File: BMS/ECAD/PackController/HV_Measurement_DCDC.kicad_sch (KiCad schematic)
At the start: 16 parts, among them U2002 TEA1-0505HI

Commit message: finalised schematic of pack controller
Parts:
- removed C2015: 100n 0603 50V, symbol Device:C
- removed U2005: (no value), symbol EKartParts:ADCMP393ARUZ
- C2001: footprint (none) -> Capacitor_SMD:C_0805_2012Metric
- C2009: footprint (none) -> Capacitor_SMD:C_0603_1608Metric
- R2003: footprint (none) -> Resistor_SMD:R_2512_6332Metric_Pad1.40x3.35mm_HandSolder
- U2001: value (none) -> ADUM3190; footprint (none) -> Package_SO:QSOP-16_3.9x4.9mm_P0.635mm

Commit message: many fixes
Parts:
- removed C2001, C2011, C2013: 1uC 0805 50V, Capacitor_SMD:C_0805_2012Metric, symbol Device:C
- removed C2009: 100n 0603 50V, Capacitor_SMD:C_0603_1608Metric, symbol Device:C
- removed R2002: 4.7MR 2512 3kV 1%, Resistor_SMD:R_2512_6332Metric_Pad1.40x3.35mm_HandSolder, symbol Device:R
- removed R2003: 39kR 2512 500V 1%, Resistor_SMD:R_2512_6332Metric_Pad1.40x3.35mm_HandSolder, symbol Device:R
- removed R2007, R2009: 10kR, Resistor_SMD:R_0603_1608Metric_Pad0.98x0.95mm_HandSolder, symbol Device:R
- removed U2001: ADUM3190, Package_SO:QSOP-16_3.9x4.9mm_P0.635mm, symbol EKartParts:ADUM3190
- added C2002, C2006: 100nC 0603 50V, Capacitor_SMD:C_0603_1608Metric, symbol Device:C
- added C2004: 100pC 0603 50V, Capacitor_SMD:C_0603_1608Metric, symbol Device:C
- added C2008: 100nC 0603 16V, Capacitor_SMD:C_0603_1608Metric, symbol Device:C
- added C2010: 1uC 0805 50V, Capacitor_SMD:C_0805_2012Metric, symbol Device:C
- added C2012: 1uC 0805 16V, Capacitor_SMD:C_0805_2012Metric, symbol Device:C
- added C2014: 1nC 0603 16V, Capacitor_SMD:C_0603_1608Metric, symbol Device:C
- added C2015: 100nF 0603 100V, Capacitor_SMD:C_0603_1608Metric_Pad1.08x0.95mm_HandSolder, symbol Device:C
- added C2016: 1uF 0805 50V, Capacitor_SMD:C_0805_2012Metric, symbol Device:C
- added R2004, R2005: 4.7MR 2512 3kV 0,1%, Resistor_SMD:R_2512_6332Metric_Pad1.40x3.35mm_HandSolder, symbol Device:R
- added R2006: 26.1kR 2512 500V 0,1%, Resistor_SMD:R_2512_6332Metric_Pad1.40x3.35mm_HandSolder, symbol Device:R
- added R2008: 1kR, Resistor_SMD:R_0603_1608Metric_Pad0.98x0.95mm_HandSolder, symbol Device:R
- added U2003: AMC0311R, EKartParts:AMC0311R Wide-body SOIC (DWV), symbol EKartParts:AMC0311R
- added U2004: LP5907MFX-3.3, Package_TO_SOT_SMD:SOT-23-5, symbol Regulator_Linear:LP5907MFX-3.3
- R2001: value 4.7MR 2512 3kV 1% -> 500R 0805; footprint Resistor_SMD:R_2512_6332Metric_Pad1.40x3.35mm_HandSolder -> Resistor_SMD:R_0805_2012Metric_Pad1.20x1.40mm_HandSolder
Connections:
- net +5V_VEHI is gone; now on net +5V_DCDC: C2003.2, C2005.1, U2002.7 (+Vout)
- net +3.3V: now also C2006.1, U2003.6 (REFIN)
- net +5V: now also C2008.1, C2012.1, U2003.8 (VDD2)
- net +5V_DCDC: now also R2001.2, U2004.1 (IN), U2004.3 (EN)
- net GND: now also C2007.2, U2002.2 (-Vin), C2006.2, C2008.2, C2012.2, C2014.2, U2003.5 (GND2)
- net TS_N_ACCU: now also R2001.1, C2002.2, C2004.2, C2010.2, C2015.1, C2016.2, R2006.2, U2003.3 (SNSN), U2003.4 (GND1), U2004.2 (GND)
- net TS_P_DCDC: now also R2004.1; no longer R2001.1
- net V_DCDC: now also C2014.1, R2008.1
- new net: R2004.2, R2005.1
- new net: C2004.1, R2005.2, R2006.1, U2003.2 (INP)
- new net: R2008.2, U2003.7 (OUT)
- new net +3.3V_DCDC: C2002.1, C2010.1, C2015.2, C2016.1, U2003.1 (VDD1), U2004.5 (OUT)
- no-connect marks 3 -> 0
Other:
- moved on the sheet: C2003, C2005, C2007, U2002

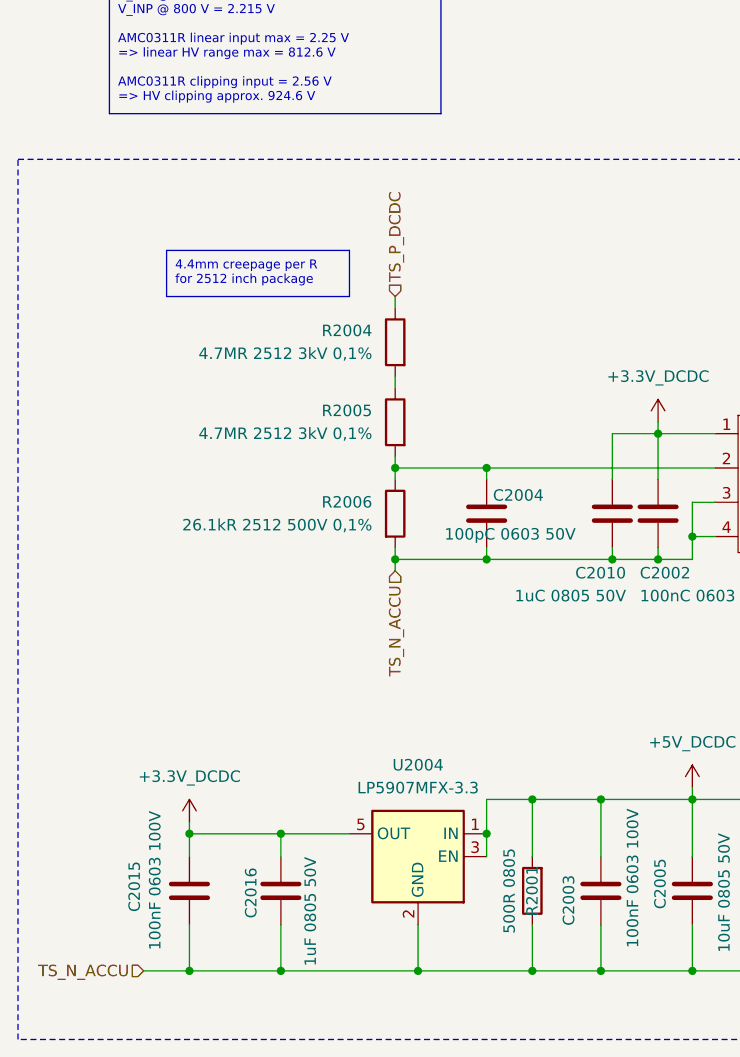
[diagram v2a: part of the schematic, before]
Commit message: add rule areas for hv separation
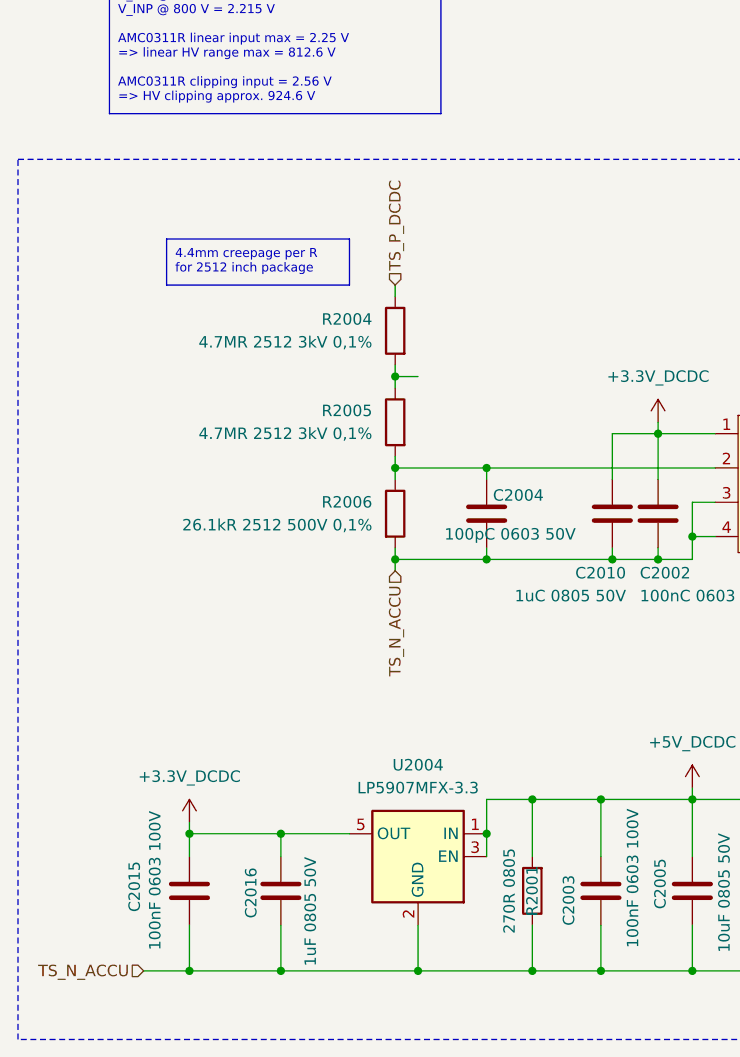
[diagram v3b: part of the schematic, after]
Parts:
- R2001: value 500R 0805 -> 270R 0805
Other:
- moved on the sheet: R2004
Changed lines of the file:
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@@
 	(text_box "4.4mm creepage per R for 2512 inch package"
 		(exclude_from_sim no)
-		(at 50.8 79.9663 0)
+		(at 50.8 78.6963 0)
 		(size 20.32 5.1237)
 		(margins 0.9525 0.9525 0.9525 0.9525)
@@
 	)
 	(junction
+		(at 76.2 93.98)
+		(diameter 0)
+		(color 0 0 0 0)
+	)
+	(junction
 		(at 109.22 140.97)
 		(diameter 0)
@@
 	(wire
 		(pts
-			(xy 76.2 85.09) (xy 76.2 86.36)
+			(xy 76.2 83.82) (xy 76.2 85.09)
 		)
 		(stroke
@@
 	(wire
 		(pts
+			(xy 76.2 93.98) (xy 78.74 93.98)
+		)
+		(stroke
+			(width 0)
+			(type default)
+		)
+	)
+	(wire
+		(pts
 			(xy 138.43 153.67) (xy 137.16 153.67)
 		)
@@
 		(pts
 			(xy 147.32 100.33) (xy 152.4 100.33)
+		)
+		(stroke
+			(width 0)
+			(type default)
+		)
+	)
+	(wire
+		(pts
+			(xy 76.2 92.71) (xy 76.2 93.98)
 		)
 		(stroke
@@
 	(hierarchical_label "TS_P_DCDC"
 		(shape input)
-		(at 76.2 85.09 90)
+		(at 76.2 83.82 90)
 		(effects
 			(font
@@
 			)
 			(justify left)
+		)
+	)
+	(netclass_flag ""
+		(length 2.54)
+		(shape round)
+		(at 86.36 104.14 0)
+		(fields_autoplaced yes)
+		(effects
+			(font
+				(size 1.27 1.27)
+			)
+			(justify left bottom)
+		)
+		(property "Netzklasse" "HV0"
+			(at 87.0585 101.6 0)
+			(show_name no)
+			(do_not_autoplace no)
+			(effects
+				(font
+					(size 1.27 1.27)
+				)
+				(justify left)
+			)
+		)
+		(property "Component Class" ""
+			(at 63.5 25.4 0)
+			(show_name no)
+			(do_not_autoplace no)
+			(effects
+				(font
+					(size 1.27 1.27)
+					(italic yes)
+				)
+			)
+		)
+	)
+	(netclass_flag ""
+		(length 2.54)
+		(shape round)
+		(at 78.74 93.98 0)
+		(fields_autoplaced yes)
+		(effects
+			(font
+				(size 1.27 1.27)
+			)
+			(justify left bottom)
+		)
+		(property "Netzklasse" "HV400"
+			(at 79.4385 91.44 0)
+			(show_name no)
+			(do_not_autoplace no)
+			(effects
+				(font
+					(size 1.27 1.27)
+				)
+				(justify left)
+			)
+		)
+		(property "Component Class" ""
+			(at 55.88 15.24 0)
+			(show_name no)
+			(do_not_autoplace no)
+			(effects
+				(font
+					(size 1.27 1.27)
+					(italic yes)
+				)
+			)
+		)
+	)
+	(netclass_flag ""
+		(length 2.54)
+		(shape round)
+		(at 63.5 144.78 0)
+		(fields_autoplaced yes)
+		(effects
+			(font
+				(size 1.27 1.27)
+			)
+			(justify left bottom)
+		)
+		(property "Netzklasse" "HV0"
+			(at 64.1985 142.24 0)
+			(show_name no)
+			(do_not_autoplace no)
+			(effects
+				(font
+					(size 1.27 1.27)
+				)
+				(justify left)
+			)
+		)
+		(property "Component Class" ""
+			(at 40.64 66.04 0)
+			(show_name no)
+			(do_not_autoplace no)
+			(effects
+				(font
+					(size 1.27 1.27)
+					(italic yes)
+				)
+			)
+		)
+	)
+	(netclass_flag ""
+		(length 2.54)
+		(shape round)
+		(at 99.06 140.97 0)
+		(fields_autoplaced yes)
+		(effects
+			(font
+				(size 1.27 1.27)
+			)
+			(justify left bottom)
+		)
+		(property "Netzklasse" "HV0"
+			(at 99.7585 138.43 0)
+			(show_name no)
+			(do_not_autoplace no)
+			(effects
+				(font
+					(size 1.27 1.27)
+				)
+				(justify left)
+			)
+		)
+		(property "Component Class" ""
+			(at 76.2 62.23 0)
+			(show_name no)
+			(do_not_autoplace no)
+			(effects
+				(font
+					(size 1.27 1.27)
+					(italic yes)
+				)
+			)
 		)
 	)
@@
 	(symbol
 		(lib_id "Device:R")
-		(at 76.2 90.17 0)
+		(at 76.2 88.9 0)
 		(mirror y)
 		(unit 1)
@@
 		(fields_autoplaced yes)
 		(property "Reference" "R2004"
-			(at 73.66 88.8999 0)
+			(at 73.66 87.6299 0)
 			(show_name no)
 			(do_not_autoplace no)
@@
 		)
 		(property "Value" "4.7MR 2512 3kV 0,1%"
-			(at 73.66 91.4399 0)
+			(at 73.66 90.1699 0)
 			(show_name no)
 			(do_not_autoplace no)
@@
 		)
 		(property "Footprint" "Resistor_SMD:R_2512_6332Metric_Pad1.40x3.35mm_HandSolder"
-			(at 77.978 90.17 90)
+			(at 77.978 88.9 90)
 			(hide yes)
 			(show_name no)
@@
 		)
 		(property "Datasheet" ""
-			(at 76.2 90.17 0)
+			(at 76.2 88.9 0)
 			(hide yes)
 			(show_name no)
@@
 		)
 		(property "Description" "Resistor"
-			(at 76.2 90.17 0)
+			(at 76.2 88.9 0)
 			(hide yes)
 			(show_name no)
@@
 			)
 		)
-		(property "Value" "500R 0805"
+		(property "Value" "270R 0805"
 			(at 88.9 151.13 90)
 			(show_name no)

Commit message: yes
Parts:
- C2005, C2007: value 10uF 0805 50V -> 10uF 0805 35V
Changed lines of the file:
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@@
 			(justify left bottom)
 		)
-		(property "Netzklasse" "HV0"
+		(property "Netclass" "HV0"
 			(at 87.0585 101.6 0)
 			(show_name no)
@@
 			(justify left bottom)
 		)
-		(property "Netzklasse" "HV400"
+		(property "Netclass" "HV400"
 			(at 79.4385 91.44 0)
 			(show_name no)
@@
 			(justify left bottom)
 		)
-		(property "Netzklasse" "HV0"
+		(property "Netclass" "HV0"
 			(at 64.1985 142.24 0)
 			(show_name no)
@@
 			(justify left bottom)
 		)
-		(property "Netzklasse" "HV0"
+		(property "Netclass" "HV0"
 			(at 99.7585 138.43 0)
 			(show_name no)
@@
 			)
 		)
-		(property "Value" "10uF 0805 50V"
+		(property "Value" "10uF 0805 35V"
 			(at 147.066 158.496 90)
 			(show_name no)
@@
 			)
 		)
-		(property "Value" "10uF 0805 50V"
+		(property "Value" "10uF 0805 35V"
 			(at 112.776 157.988 90)
 			(show_name no)
